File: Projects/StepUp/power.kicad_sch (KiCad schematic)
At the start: 62 parts, among them Q3 PMF170XP,115, Q4 2N7002-7-F, Q5 SSM3J328R_LF, Q6 2N7002-7-F, SW3 1825027-8, U5 LDL1117S33R, U6 MCP73832T-2ACI_OT, U7 MIC2253, U8 ECH8697R-TL-W, U9 BQ2970

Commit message: feat(v0.2): Release, PCBs ordered!
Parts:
- added J6: Conn_01x05, Connector_PinHeader_2.54mm:PinHeader_1x05_P2.54mm_Vertical, symbol Connector_Generic:Conn_01x05
- BT1, BT2: MPN (none) -> 54; Manufacturer (none) -> Krystone Electronics; now in the parts list
- C35: footprint Capacitor_SMD:C_0603_1608Metric -> Capacitor_SMD:C_0805_2012Metric; Dielectric (none) -> X7R; MPN (none) -> CL21B105KAFNNNE; Manufacturer (none) -> Samsung Electro-Mechanics; Package 0603 -> 0805; Tolerance 20% -> 10%; Voltage (none) -> 25V
- Q5: MPN (none) -> SSM3J328R,LF; Manufacturer (none) -> Toshiba Semiconductor and Storage
- R23: MPN (none) -> RC1206FR-070RL; Manufacturer (none) -> YAGEO; Tolerance 1% -> (none)
- R24: value 2.7kR -> 2.49kR; MPN RC0603FR-072KL -> ERJ-3EKF2491V; Manufacturer YAGEO -> Panasonic
- R32: MPN (none) -> RC0603FR-070RL; Manufacturer (none) -> YAGEO; Tolerance 1% -> (none)
- R33: MPN (none) -> RC0603FR-071ML; Manufacturer (none) -> YAGEO; Tolerance 0.5% -> 1%
- R36: MPN (none) -> RC0603FR-07330RL; Manufacturer (none) -> YAGEO; Tolerance (none) -> 1%
- R37: MPN (none) -> RC0603FR-070RL; Manufacturer (none) -> YAGEO; Tolerance 0.5% -> (none)
- R38, R48: MPN (none) -> RC0603FR-075M1L; Manufacturer (none) -> YAGEO; Tolerance (none) -> 1%
- R44: MPN RT0603DRE10100KL -> RC0603FR-0756KL
- R46: MPN (none) -> RC0603FR-072K2L; Manufacturer (none) -> YAGEO; Tolerance 0.5% -> 1%
- R47: MPN (none) -> RC0603FR-07100RL; Manufacturer (none) -> YAGEO; Tolerance (none) -> 1%
- SW3: MPN (none) -> 1825027-8; Manufacturer (none) -> TE Connectivity
- U9: MPN BQ2970 -> BQ29706DSER
- renumbered LED1 to D12, D12 to D13, D13 to D14
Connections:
- net +3V3: now also J6.4 (Pin_4)
- net GND: now also J6.5 (Pin_5)
- net VMotor: now also J6.3 (Pin_3)
- net V_USB: now also J6.1 (Pin_1)
- net Vbat: now also J6.2 (Pin_2)
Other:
- note added: "I_REG = 1000 V / 2.49 (kR) I_REG = ~400 mA"
- note added: "Voltage test pads"
- note removed: "I_REG = 1000 V / 2.7 (kR) I_REG = 370 mA"
- moved on the sheet: BT1, BT2

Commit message: feat(v0.3): Begin work on next rev
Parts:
- removed JP1: SolderJumper_2_Bridged, Jumper:SolderJumper-2_P1.3mm_Bridged2Bar_RoundedPad1.0x1.5mm, symbol Jumper:SolderJumper_2_Bridged
- removed R21: 100kR, Resistor_SMD:R_0603_1608Metric, symbol Device:R
- removed R34: 100R, Resistor_SMD:R_0603_1608Metric, symbol Device:R
- added BT3: 54, Samacsys:54, symbol Samacsys:54
- added C36: 10uF, Capacitor_SMD:C_0805_2012Metric, symbol Device:C
- added D15: 1N4148W-TP, digikey-footprints:SOD-123, symbol dk_Diodes-Rectifiers-Single:1N4148W-TP
- added R36: 10kR, Resistor_SMD:R_0603_1608Metric, symbol Device:R
- added R57: 100kR, Resistor_SMD:R_0603_1608Metric, symbol Device:R
- R24: value 2.49kR -> 3.3kR; MPN ERJ-3EKF2491V -> ERJU03F3301V
- R35: MPN RT0603DRE10100KL -> RC0603FR-07100KL; Tolerance 0.5% -> 1%
- U9: value BQ2970 -> BQ29700; MANUFACTURER (none) -> Ti; MPN BQ29706DSER -> BQ29700DSER
- renumbered C36 to C37, C37 to C38, C38 to C39, C39 to C40, J6 to J5, R36 to R37, R37 to R38, R38 to R39, R39 to R40, R40 to R41, R41 to R42, R42 to R43, R43 to R44, R44 to R45, R45 to R46, R46 to R47, R47 to R48, R48 to R49
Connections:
- net GND: now also C36.2, R57.2
- net MCU_PWR_CTRL: now also D15.K; no longer R35.2
- net VBAT_PACK_NEG: now also BT3.1, BT3.2, BT3.3
- net V_USB: now also D11.2 (A), R22.1, R57.1
- net at Q4.1 (G): now also R35.2, C36.1, R36.1
- new net: D15.A, R36.2
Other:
- note added: "2 battery clip connectors Option: BT2 - battery of length ~65mm, no internal protection OR BT3 - battery of length ~67mm, with internal protection"
- note added: "65mm battery NO internal protection"
- note added: "67mm battery WITH internal protection"
- note added: "Common voltages"
- note added: "Default: 3v3 powered by Vbat USB inserted: 3v3 powered by Vusb"
- note added: "I_REG = 1000 V / 3.3 (kR) I_REG = ~300 mA"
- note added: "OR"
- note added: "Pull up to 3v3 as MCU reset shouldn't power OFF circuit Diode prevents MCU in RESET from fully pulling gate to 0V"
- note removed: "2 battery clip connectors"
- note removed: "Default: 3v3 powered by Vbat & Vusb when USB inserted Alt: Cut jumper to only power via Vbat"
- note removed: "I_REG = 1000 V / 2.49 (kR) I_REG = ~400 mA"
- note removed: "Pull up to 3v3 as MCU reset shouldn't power OFF circuit"
- moved on the sheet: BT1, BT2, C35, D14, Q4, Q5, R33, R35, R38, SW3

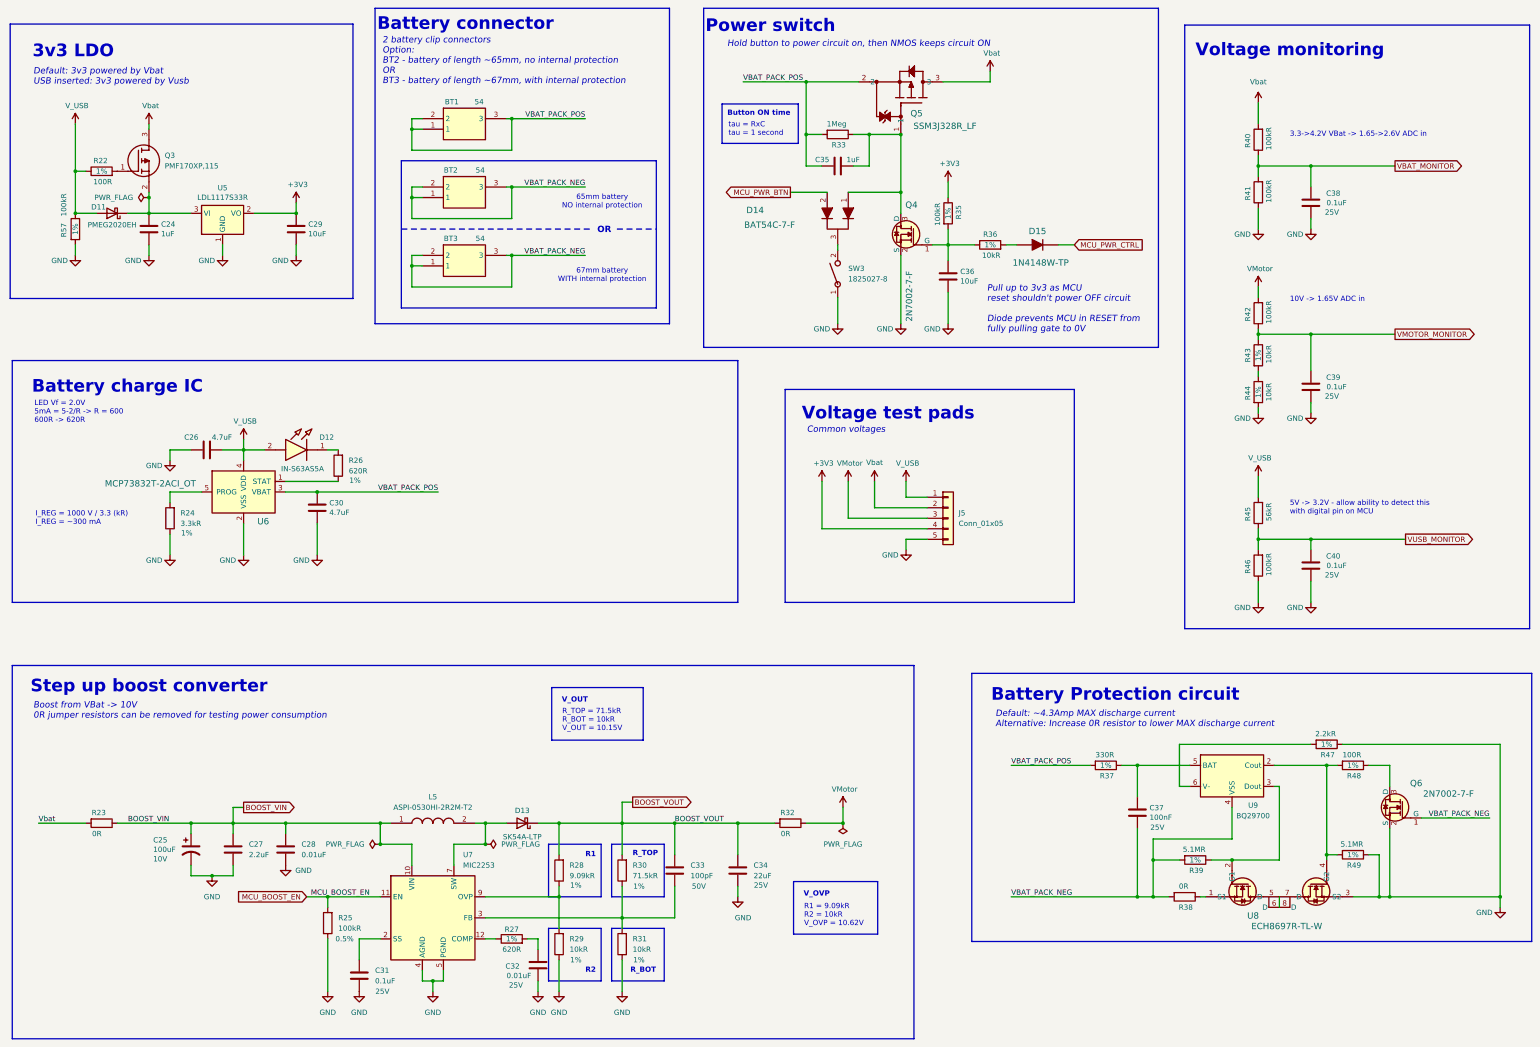
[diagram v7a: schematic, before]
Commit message: feat(v0.3): Boost layout complete
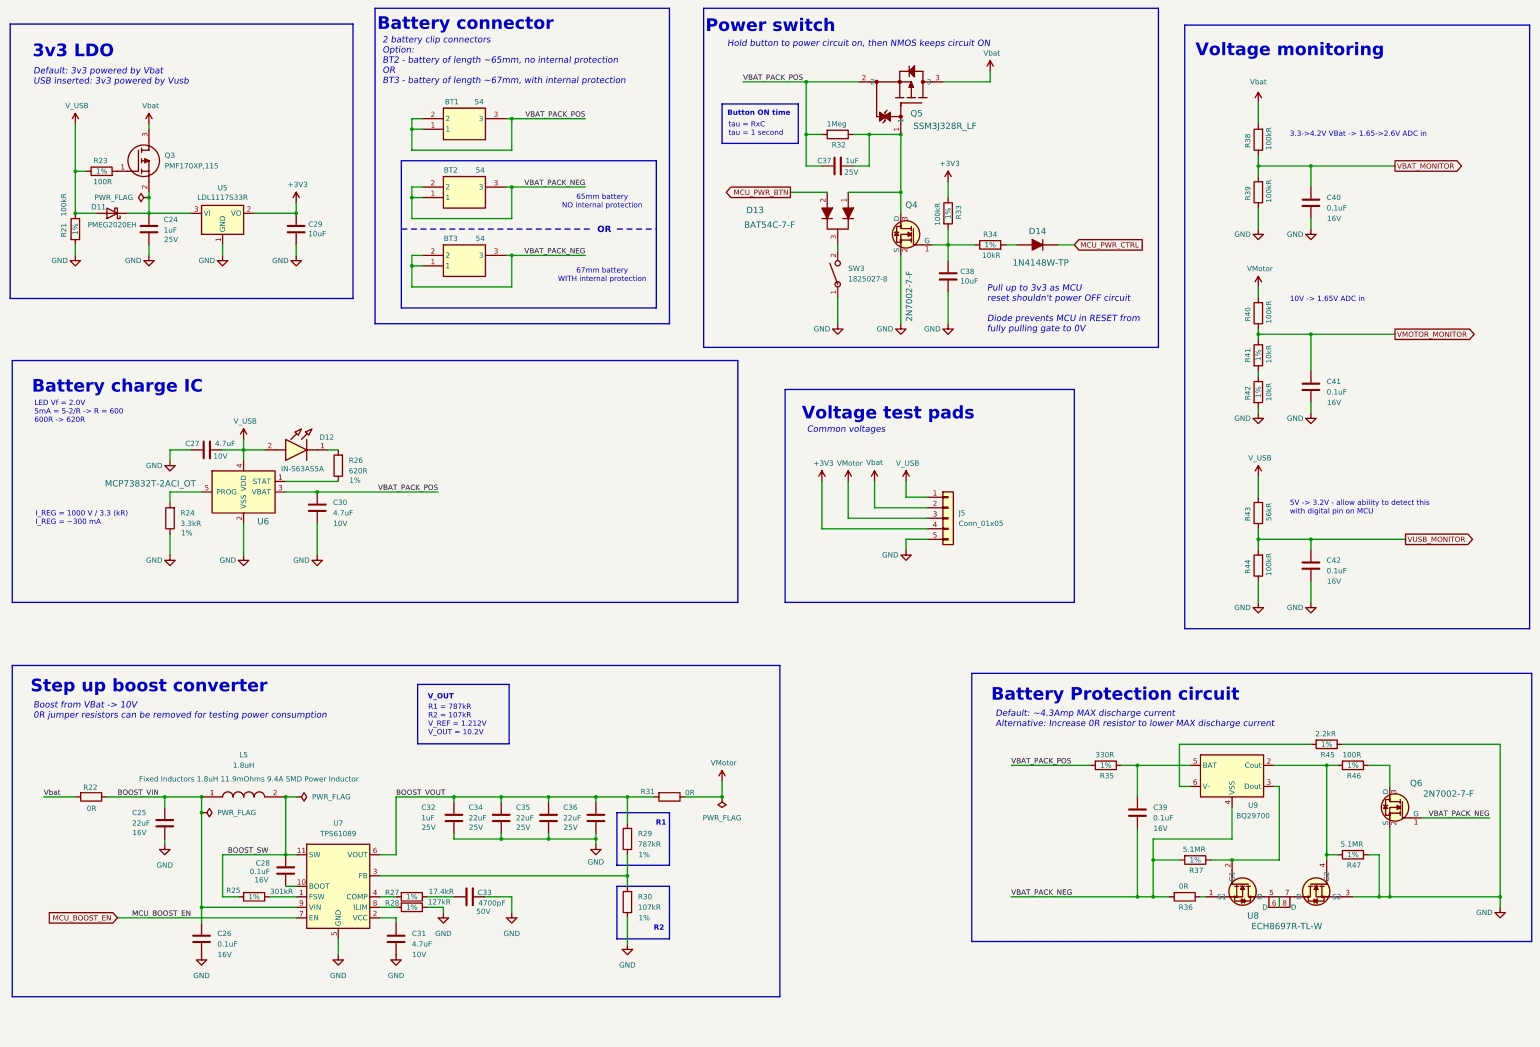
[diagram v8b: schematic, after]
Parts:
- removed C25: 100uF, Capacitor_Tantalum_SMD:CP_EIA-3528-12_Kemet-T, symbol Device:C_Polarized_US
- removed C26: 4.7uF, Capacitor_SMD:C_0805_2012Metric, symbol Device:C
- removed C38: 0.1uF, Capacitor_SMD:C_0603_1608Metric, symbol Device:C
- removed D13: SK54A-LTP, Diode_SMD:D_SMA, symbol Device:D_Schottky
- removed L5: ASPI-0530HI-2R2M-T2, Samacsys:INDPM5652X300N, symbol Samacsys:ASPI-0530HI-2R2M-T2
- removed R23: 0R, Resistor_SMD:R_1206_3216Metric, symbol Device:R
- removed R32: 0R, Resistor_SMD:R_0603_1608Metric, symbol Device:R
- removed U7: MIC2253, Package_DFN_QFN:DFN-12-1EP_3x3mm_P0.5mm_EP1.6x2.5mm_ThermalVias, symbol Regulator_Switching:MIC2253
- added C25: 22uF, Capacitor_SMD:C_1206_3216Metric, symbol Device:C
- added C31: 4.7uF, Capacitor_SMD:C_0603_1608Metric, symbol Device:C
- added C36: 22uF, Capacitor_SMD:C_1210_3225Metric, symbol Device:C
- added C41, C42: 0.1uF, Capacitor_SMD:C_0402_1005Metric, symbol Device:C
- added L5: 1.8uH, Samacsys:INDPM9585X300N, symbol Samacsys:CDMC8D28NP-1R8MC
- added R22: 0R, Resistor_SMD:R_0603_1608Metric, symbol Device:R
- added U7: TPS61089, Package_DFN_QFN:Texas_VQFN-RNR0011A-11, symbol Regulator_Switching:TPS61089
- C24: footprint Capacitor_SMD:C_0805_2012Metric -> Capacitor_SMD:C_0603_1608Metric; MPN CL21B105KAFNNNE -> GRM188R71E105KA12D; Manufacturer Samsung Electro-Mechanics -> Murata; Package 0805 -> 0603
- C26: renamed from C31; footprint Capacitor_SMD:C_0603_1608Metric -> Capacitor_SMD:C_0402_1005Metric; Dielectric X7R -> X5R; MPN CC0603KRX7R8BB104 -> GRM155R61C104KA88D; Manufacturer YAGEO -> Murata; Package 0603 -> 0402; Voltage 25V -> 16V
- C27: value 2.2uF -> 4.7uF; MPN CC0603MRX5R5BB225 -> 0603ZD475KAT2A; Manufacturer YAGEO -> AVX; Tolerance 20% -> 10%; Voltage 6.3V -> 10V
- C28: value 0.01uF -> 0.1uF; footprint Capacitor_SMD:C_0603_1608Metric -> Capacitor_SMD:C_0402_1005Metric; Dielectric X7R -> X5R; MPN CC0603JRX7R8BB103 -> GRM155R61C104KA88D; Manufacturer YAGEO -> Murata; Package 0603 -> 0402; Tolerance 5% -> 10%; Voltage 25V -> 16V
- C30: footprint Capacitor_SMD:C_0805_2012Metric -> Capacitor_SMD:C_0603_1608Metric; MPN CC0805MKX5R6BB475 -> 0603ZD475KAT2A; Manufacturer YAGEO -> AVX; Package 0805 -> 0603; Tolerance 20% -> 10%
- C32: value 0.01uF -> 1uF; MPN CC0603JRX7R8BB103 -> GRM188R71E105KA12D; Manufacturer YAGEO -> Murata; Tolerance 5% -> 10%
- C33: value 100pF -> 4700pF; footprint Capacitor_SMD:C_0603_1608Metric -> Capacitor_SMD:C_0402_1005Metric; Dielectric C0G, NP0 -> X5R; MPN CC0603JRNPO9BN101 -> GRM155R61H472KA01D; Manufacturer YAGEO -> Murata; Package 0603 -> 0402; Tolerance 5% -> 10%
- C34: footprint Capacitor_SMD:C_0805_2012Metric -> Capacitor_SMD:C_1210_3225Metric; Dielectric X5R -> X7R; MPN CC0805MKX5R8BB226 -> GRM32ER71E226KE15L; Manufacturer YAGEO -> Murata; Package 0805 -> 1210; Tolerance 20% -> 10%
- C35: value 1uF -> 22uF; footprint Capacitor_SMD:C_0805_2012Metric -> Capacitor_SMD:C_1210_3225Metric; MPN CL21B105KAFNNNE -> GRM32ER71E226KE15L; Manufacturer Samsung Electro-Mechanics -> Murata; Package 0805 -> 1210
- C37: value 100nF -> 1uF; footprint Capacitor_SMD:C_0402_1005Metric -> Capacitor_SMD:C_0603_1608Metric; MPN CC0402KRX7R8BB104 -> GRM188R71E105KA12D; Manufacturer YAGEO -> Murata; Package 0402 -> 0603
- C39, C40: footprint Capacitor_SMD:C_0603_1608Metric -> Capacitor_SMD:C_0402_1005Metric; Dielectric X7R -> X5R; MPN CC0603KRX7R8BB104 -> GRM155R61C104KA88D; Manufacturer YAGEO -> Murata; Package 0603 -> 0402; Voltage 25V -> 16V
- R25: value 100kR -> 301kR; footprint Resistor_SMD:R_0603_1608Metric -> Resistor_SMD:R_0402_1005Metric; MPN RT0603DRE10100KL -> CRCW0402301KFKED; Manufacturer YAGEO -> Vishay-Dale; Package 0603 -> 0402; Power 0.1W, 1/10W -> 0.063W, 1/16W; Tolerance 0.5% -> 1%
- R27: value 620R -> 17.4kR; footprint Resistor_SMD:R_0603_1608Metric -> Resistor_SMD:R_0402_1005Metric; MPN RC0603FR-07620RL -> CRCW040217K4FKED; Manufacturer YAGEO -> Vishay-Dale; Package 0603 -> 0402; Power 0.1W, 1/10W -> 0.063W, 1/16W
- R28: value 9.09kR -> 127kR; footprint Resistor_SMD:R_0603_1608Metric -> Resistor_SMD:R_0402_1005Metric; MPN RC0603FR-079K09L -> CRCW0402127KFKED; Manufacturer YAGEO -> Vishay-Dale; Package 0603 -> 0402; Power 0.1W, 1/10W -> 0.063W, 1/16W
- R29: value 10kR -> 787kR; footprint Resistor_SMD:R_0603_1608Metric -> Resistor_SMD:R_0402_1005Metric; MPN RC0603FR-0710KL -> CRCW0402787KFKED; Manufacturer YAGEO -> Vishay-Dale; Package 0603 -> 0402; Power 0.1W, 1/10W -> 0.063W, 1/16W
- R30: value 71.5kR -> 107kR; footprint Resistor_SMD:R_0603_1608Metric -> Resistor_SMD:R_0402_1005Metric; MPN RC0603FR-0771K5L -> CRCW0402107KFKED; Manufacturer YAGEO -> Vishay-Dale; Package 0603 -> 0402; Power 0.1W, 1/10W -> 0.063W, 1/16W
- R31: value 10kR -> 0R; MPN RC0603FR-0710KL -> RC0603FR-070RL; Tolerance 1% -> (none)
- renumbered C36 to C38, D14 to D13, D15 to D14, R57 to R21, R22 to R23, R33 to R32, R35 to R33, R36 to R34, R37 to R35, R38 to R36, R39 to R37, R40 to R38, R41 to R39, R42 to R40, R43 to R41, R44 to R42, R45 to R43, R46 to R44, R47 to R45, R48 to R46, R49 to R47
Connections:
- net BOOST_VIN: now also C26.1, C25.1, L5.1, R22.1, U7.9 (VIN); no longer C27.1, C28.1
- net BOOST_VOUT: now also C32.1, C35.1, R29.2, R31.2, C36.1, U7.6 (VOUT); no longer C33.1, R28.2, R30.2
- net GND: now also C27.1, C33.2, C35.2, C40.2, R28.1, R30.1, C25.2, C31.2, C36.2, C41.2, C42.2, U7.5 (GND); no longer C27.2, C28.2, C39.1, C40.1, R25.1, R29.1, R31.1
- net MCU_BOOST_EN: now also U7.7 (EN); no longer R25.2
- net VBAT_MONITOR: now also C40.1
- net VBAT_PACK_NEG: now also C39.2; no longer C37.2
- net VBAT_PACK_POS: now also C37.1; no longer C35.1
- net VMOTOR_MONITOR: now also C41.1; no longer C39.2
- net VMotor: now also R31.1
- net VUSB_MONITOR: now also C42.1; no longer C40.2
- net V_USB: now also C27.2
- net Vbat: now also R22.2
- net at R27.1: now also C33.1
- net at D13.1, Q4.3 (D), Q5.1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: now also C37.2; no longer C35.2
- net at R35.1, U9.5 (BAT): now also C39.1; no longer C37.1
- net at R27.2: now also U7.4 (COMP); no longer C32.1
- new net: R29.1, R30.2, U7.3 (FB)
- new net: R25.1, U7.1 (FSW)
- new net: C28.1, U7.10 (BOOT)
- new net: C31.1, U7.2 (VCC)
- new net: R28.2, U7.8 (ILIM)
- new net BOOST_SW: C28.2, L5.2, R25.2, U7.11 (SW)
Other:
- note added: "R1 = 787kR R2 = 107kR V_REF = 1.212V V_OUT = 10.2V"
- note removed: "R1 = 9.09kR R2 = 10kR V_OVP = 10.62V"
- note removed: "R_BOT"
- note removed: "R_TOP"
- note removed: "R_TOP = 71.5kR R_BOT = 10kR V_OUT = 10.15V"
- note removed: "V_OVP"
- moved on the sheet: C26
